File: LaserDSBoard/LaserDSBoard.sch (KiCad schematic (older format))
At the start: 185 parts, among them J1 JTAG, J10 D SWITCH, J11 LASER, J12 Y VREF, J13 X VREF, J14 Y1 MOTOR, J15 X MOTOR, J16 Y2 MOTOR, J17 Y VREF, J2 USB, J3 POWER IN, J4 LASER P, J5 X LIMIT1, J6 WATER FLOW, J7 X LIMIT2, J8 Y LIMIT1, J9 Y LIMIT2, SW1 DHT-1163S, SW2 SSSS213202, U1 LD1117S, U10 TLP2355, U11 ADUM1250, U12 TLP2355, U13 TLP2355, U14 TLP2355, U15 TLP2355, U16 TLP2355, U17 TLP2355, U18 TLP2355, U19 MCP3425, U2 LD1117S, U20 A4982SLPTR, U21 A4982SLPTR, U22 TLP2355, U23 TPL0401A, U24 TPL0401B, U25 A4982SLPTR, U3 STM32F20XR, U4 LD1117S, U5 ADUM1250, U6 TLP2355, U7 TLP2355, U8 TLP2355, U9 TLP2355, X1 7B-25.000MAAJ-T, X2 9HT10-32.768KDZY-T

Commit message: Ver2.0.0
[schematic]
・デジタルポテンショメータ　MCP4461に戻す
・フォトカプラ ENの経路(U14,U17,U29)
TLP2355→TLP291に変更

[AW]
・回路図変更に伴うAW変更
・モータドライバ回りビア増加
・SW2の向きを反転
・部品実装マークをシルクで追加
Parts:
- removed C29: 0u1, Capacitors_SMD:C_0805, symbol C-RESCUE-LaserDSBoard
- removed J10: D SWITCH, mylib:S3B-XH-SM4-TB, symbol CONN3
- removed J5: X LIMIT1, mylib:S3B-XH-SM4-TB, symbol CONN3
- removed J7: X LIMIT2, mylib:S3B-XH-SM4-TB, symbol CONN3
- removed J8: Y LIMIT1, mylib:S3B-XH-SM4-TB, symbol CONN3
- removed J9: Y LIMIT2, mylib:S3B-XH-SM4-TB, symbol CONN3
- removed R19, R20, R23, R24, R32: 1k, Resistors_SMD:R_0603, symbol R-RESCUE-LaserDSBoard
- removed U14, U17: TLP2355, mylib:TLP2355, symbol TLP2355
- removed U23: TPL0401A, mylib:TPL0401, symbol TPL0401X
- removed U24: TPL0401B, mylib:TPL0401, symbol TPL0401X
- added J10: D SWITCH, mylib:B2B-XH-A, symbol CONN2
- added J5: X LIMIT1, mylib:B2B-XH-A, symbol CONN2
- added J7: X LIMIT2, mylib:B2B-XH-A, symbol CONN2
- added J8: Y LIMIT1, mylib:B2B-XH-A, symbol CONN2
- added J9: Y LIMIT2, mylib:B2B-XH-A, symbol CONN2
- added R43, R44, R45: 220R, Resistors_SMD:R_1206, symbol R-RESCUE-LaserDSBoard
- added U14, U17, U29: TLP291, mylib:TLP291(SE, symbol TLP291
- added U23: MCP4461, Package_SO:TSSOP-20_4.4x6.5mm_P0.65mm, symbol MCP44X1
- added U27, U28: TLP2355, mylib:TLP2355, symbol TLP2355
- D1, D10, D2, D3, D4, D5, D6, D7, D8, D9: footprint Diodes_SMD:D_0603 -> Diodes_SMD:D_0805
- J1: footprint Pin_Headers:Pin_Header_Straight_2x05_Pitch1.00mm -> Pin_Headers:Pin_Header_Straight_2x05_Pitch1.27mm
- J11, J6: footprint mylib:S3B-XH-SM4-TB -> mylib:B3B-XH-A
- J4: footprint mylib:S3B-XH-SM4-TB -> mylib:B2B-XH-A
- R18: value 1k -> 10k
- R65: value 1k5 -> 2k4
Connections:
- net +3V3: now also C24.2, R18.1, U23.17 (VDD), U27.6, U28.6; no longer C24.1
- net D+3.3V: no longer R18.1
- net GNDA: now also C24.1, R51.1, J10.2 (PM), J5.2 (PM), J7.2 (PM), J8.2 (PM), J9.2 (PM), U14.3, U17.3, U23.13 (P0B), U23.16 (A1), U23.3 (P3B), U23.4 (HVC/A0), U23.7 (VSS), U23.8 (P1B), U27.4, U28.4, U29.3; no longer C24.2, U22.3
- net GNDD: now also R55.2, R56.2, R57.2, R58.2, R59.2, R6.2, R60.2, R43.2, R44.2, R45.2; no longer U12.3, U13.3, U15.3, U16.3, U6.3
- net LASER_OUT: now also U6.1; no longer R6.2
- net X_DIR: now also U16.1; no longer R59.2
- net X_EN: now also U17.1; no longer R60.2
- net X_LIMIT1: no longer R18.2
- net X_REF: now also U23.12 (P0W)
- net X_STEP: now also U15.1; no longer R58.2
- net at R39.2: now also U23.1 (P3A), U23.10 (P1A), U23.11 (P0A)
- net at R38.2, U5.7 (SDA2): now also U23.6 (SDA)
- net at R36.2, U5.6 (SCL2): now also U23.5 (SCL)
- net at R68.2, U21.23 (/ENABLE): now also U17.4
- net at D9.2 (K), U18.3: now also J10.1 (P1)
- net Y2_STEP: now reaches U3.51 (PC10)
- net Y2_STEP: now also U27.1
- net Y2_DIR: now reaches U3.52 (PC11)
- net Y2_DIR: now also U28.1
- net Y2_EN: now reaches U3.53 (PC12)
- net Y2_EN: now also U29.1
- net at J6.3 (P3): now also U22.1; no longer R51.1
- net at R51.2: now also U22.3; no longer U22.1
- net at R59.1: now also U16.3; no longer U16.1
- net at R58.1: now also U15.3; no longer U15.1
- net at R60.1: now also U17.2
- net at R56.1: now also U13.3; no longer U13.1
- net at R55.1: now also U12.3; no longer U12.1
- net at R57.1: now also U14.2
- net at D5.2 (K), U7.3: now also J5.1 (P1)
- net at D6.2 (K), U8.3: now also J7.1 (P1)
- net at D7.2 (K), U9.3: now also J8.1 (P1)
- net at D8.2 (K), U10.3: now also J9.1 (P1)
- net at R6.1: now also U6.3; no longer U6.1
- net Y_DIR renamed Y1_DIR
- net Y1_DIR: now also U13.1; no longer R56.2
- net Y_DIR_A renamed Y1_DIR_A
- net Y1_DIR_A: no longer U25.14 (DIR)
- net Y_EN renamed Y1_EN
- net Y1_EN: now also U14.1; no longer R57.2
- net Y_EN_A renamed Y1_EN_A
- net Y1_EN_A: now also U14.4; no longer R34.2, U25.23 (/ENABLE)
- net Y_REF renamed Y1_REF
- net Y1_REF: now also U23.9 (P1W); no longer C56.1, J17.1 (Vref), U25.12 (REF)
- net Y_STEP renamed Y1_STEP
- net Y1_STEP: now also U12.1; no longer R55.2
- net Y_STEP_A renamed Y1_STEP_A
- net Y1_STEP_A: no longer U25.11 (STEP)
- new net: R44.1, U28.3
- new net: R43.1, U27.3
- new net: R45.1, U29.2
- new net: R18.2, U23.15 (*RESET)
- new net Y2_DIR_A: U25.14 (DIR), U28.5
- new net Y2_EN_A: R34.2, U25.23 (/ENABLE), U29.4
- new net Y2_REF: C56.1, J17.1 (Vref), U23.2 (P3W), U25.12 (REF)
- new net Y2_STEP_A: U25.11 (STEP), U27.5
- no-connect marks 25 -> 26
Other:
- note added: "0: Normal Mode\n1: DFU Mode"
- moved on the sheet: C18, C24, C27, C30, C31, C32, C33, C35, C37, C39, C40, C42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

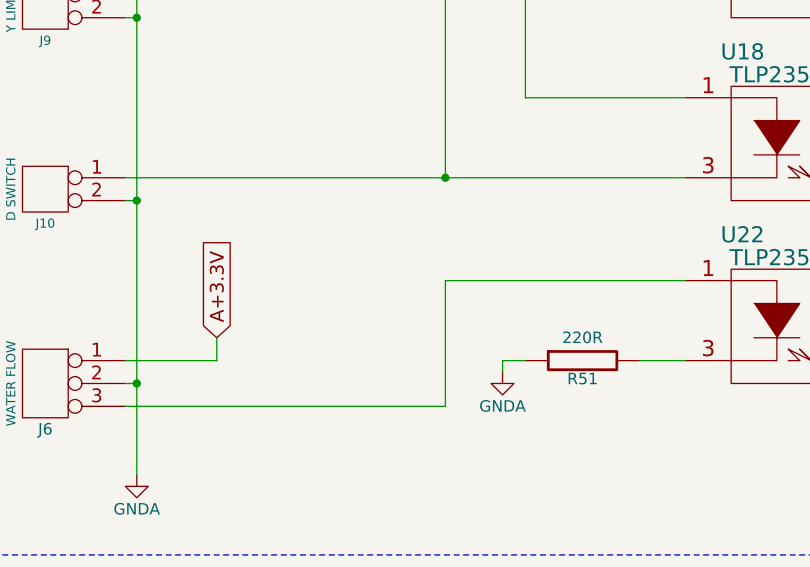
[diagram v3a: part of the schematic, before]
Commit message: Ver2.0.1
・WATER FLOW　電源をA+3.3V→A+5.0Vにつなぎ変え
・R51 抵抗値変更
220Ω→160Ω
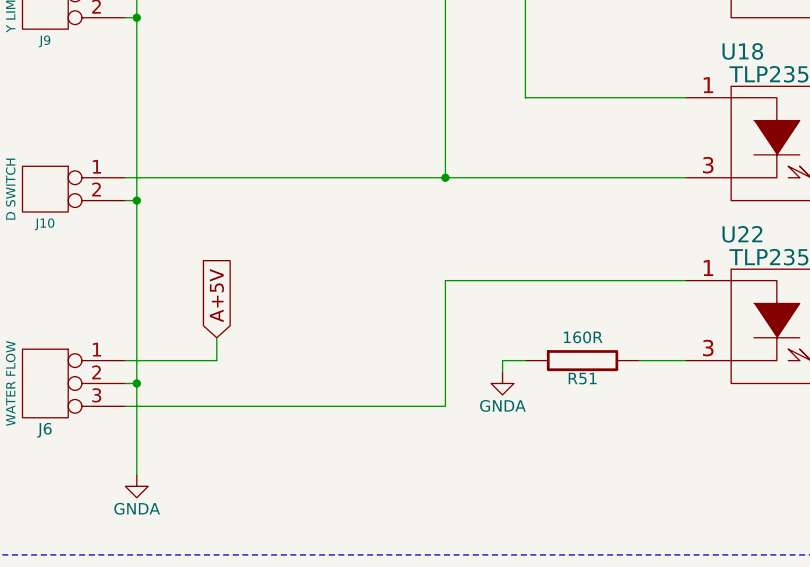
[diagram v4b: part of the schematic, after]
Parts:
- R51: value 220R -> 160R
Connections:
- net +3V3: no longer J6.1 (P1)
- net +5VA: now also J6.1 (P1)
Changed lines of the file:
@@
 Sheet 1 1
 Title "LaserDSBoard"
-Date "2018-04-10"
-Rev "2.0.0"
+Date "2018-05-19"
+Rev "2.0.1"
 Comp "smartDIYs Co.,Ltd."
 Comment1 "http://www.smartdiys.com/"
@@
 	0    1    1    0
 $EndComp
-Text GLabel 7350 6300 1    60   Input ~ 0
-A+3.3V
 $Comp
 L R-RESCUE-LaserDSBoard R51
@@
 P 8950 6400
 F 0 "R51" V 9030 6400 50  0000 C CNN
-F 1 "220R" V 8850 6400 50  0000 C CNN
+F 1 "160R" V 8850 6400 50  0000 C CNN
 F 2 "Resistors_SMD:R_1206" H 8950 6400 60  0001 C CNN
 F 3 "" H 8950 6400 60  0001 C CNN
@@
 Wire Notes Line
 	5450 11000 4650 11000
+Text GLabel 7350 6300 1    60   Input ~ 0
+A+5V
 $EndSCHEMATC
